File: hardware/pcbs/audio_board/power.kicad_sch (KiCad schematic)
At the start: 31 parts, among them Q1 S8050, U2 LP5907MFX-3.3, U3 LM5158

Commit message: prepare for clock fanout
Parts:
- renumbered R12 to R20, R13 to R21, R14 to R22, R15 to R23, R16 to R24, R17 to R25, R18 to R26

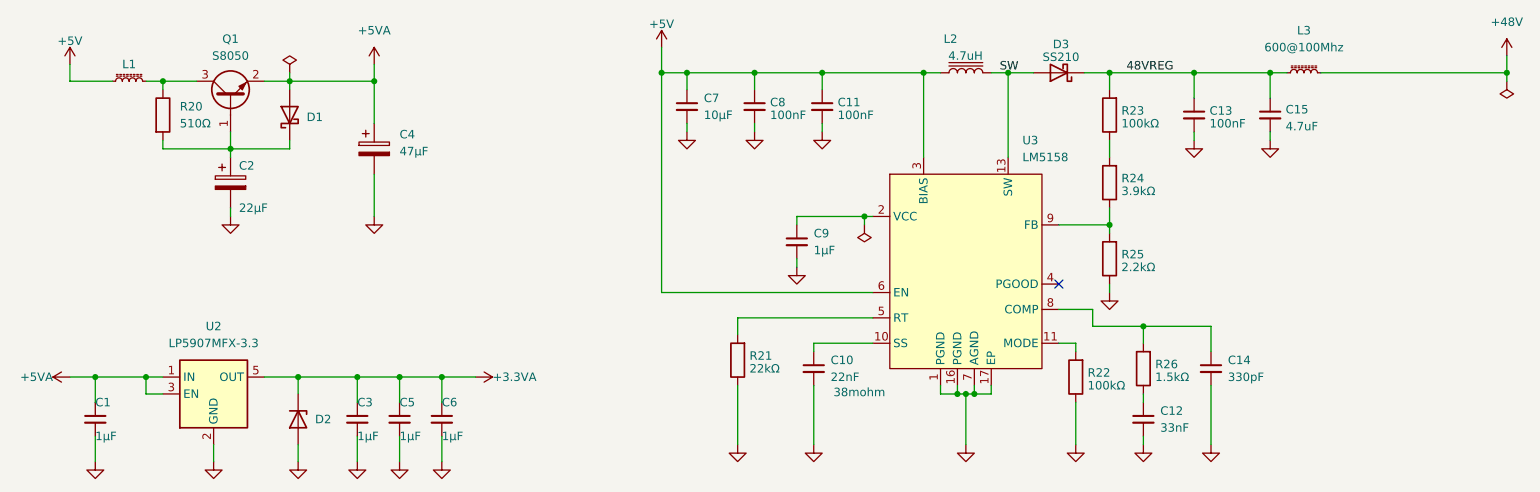
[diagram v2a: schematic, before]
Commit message: audioboard: route clock fanout
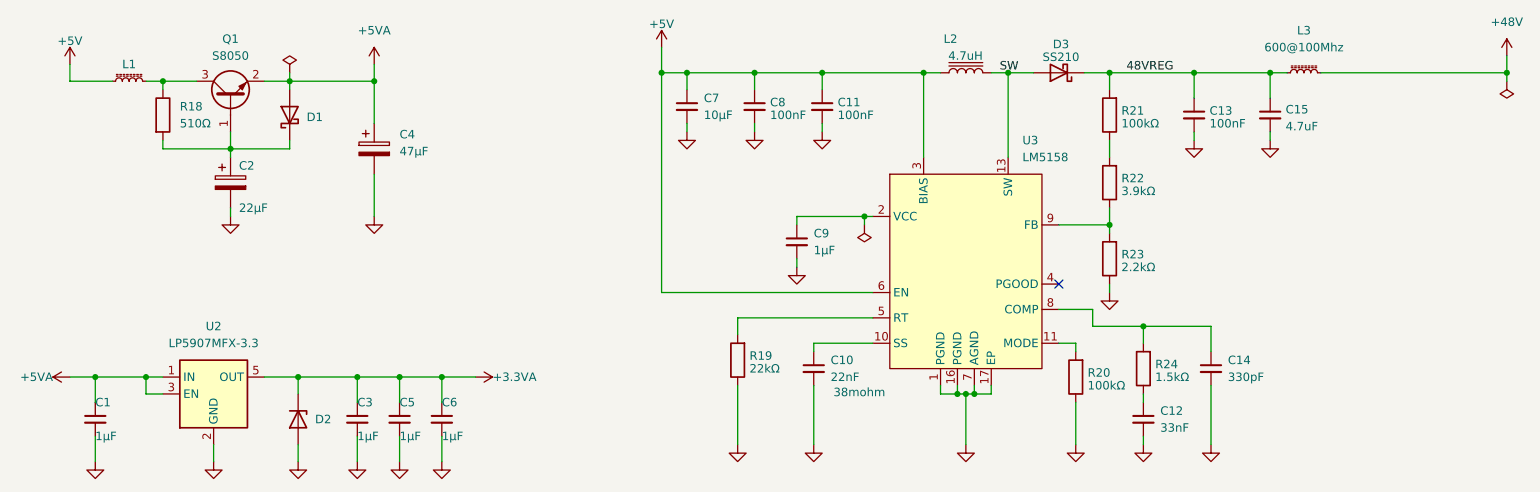
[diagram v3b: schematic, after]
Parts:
- renumbered R20 to R18, R21 to R19, R22 to R20, R23 to R21, R24 to R22, R25 to R23, R26 to R24
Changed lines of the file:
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@@
 		(in_pos_files yes)
 		(dnp no)
-		(property "Reference" "R21"
+		(property "Reference" "R19"
 			(at 147.828 104.7663 0)
 			(show_name no)
@@
 			(project "audio_board"
 				(path "/54443f96-c7c5-4432-b890-45b14a1547a1/23b45e70-9f0d-43c3-ad82-81d9481de3a2"
-					(reference "R21")
+					(reference "R19")
 					(unit 1)
 				)
@@
 		(in_pos_files yes)
 		(dnp no)
-		(property "Reference" "R22"
+		(property "Reference" "R20"
 			(at 198.628 107.3063 0)
 			(show_name no)
@@
 			(project "audio_board"
 				(path "/54443f96-c7c5-4432-b890-45b14a1547a1/23b45e70-9f0d-43c3-ad82-81d9481de3a2"
-					(reference "R22")
+					(reference "R20")
 					(unit 1)
 				)
@@
 		(in_pos_files yes)
 		(dnp no)
-		(property "Reference" "R26"
+		(property "Reference" "R24"
 			(at 208.788 106.0363 0)
 			(show_name no)
@@
 			(project "audio_board"
 				(path "/54443f96-c7c5-4432-b890-45b14a1547a1/23b45e70-9f0d-43c3-ad82-81d9481de3a2"
-					(reference "R26")
+					(reference "R24")
 					(unit 1)
 				)
@@
 		(in_pos_files yes)
 		(dnp no)
-		(property "Reference" "R25"
+		(property "Reference" "R23"
 			(at 203.708 89.5263 0)
 			(show_name no)
@@
 			(project "audio_board"
 				(path "/54443f96-c7c5-4432-b890-45b14a1547a1/23b45e70-9f0d-43c3-ad82-81d9481de3a2"
-					(reference "R25")
+					(reference "R23")
 					(unit 1)
 				)
@@
 		(in_pos_files yes)
 		(dnp no)
-		(property "Reference" "R24"
+		(property "Reference" "R22"
 			(at 203.708 78.0963 0)
 			(show_name no)
@@
 			(project "audio_board"
 				(path "/54443f96-c7c5-4432-b890-45b14a1547a1/23b45e70-9f0d-43c3-ad82-81d9481de3a2"
-					(reference "R24")
+					(reference "R22")
 					(unit 1)
 				)
@@
 		(in_pos_files yes)
 		(dnp no)
-		(property "Reference" "R23"
+		(property "Reference" "R21"
 			(at 203.708 67.9363 0)
 			(show_name no)
@@
 			(project "audio_board"
 				(path "/54443f96-c7c5-4432-b890-45b14a1547a1/23b45e70-9f0d-43c3-ad82-81d9481de3a2"
-					(reference "R23")
+					(reference "R21")
 					(unit 1)
 				)
@@
 		(dnp no)
 		(fields_autoplaced yes)
-		(property "Reference" "R20"
+		(property "Reference" "R18"
 			(at 62.23 67.3099 0)
 			(show_name no)
@@
 			(project "audio_board"
 				(path "/54443f96-c7c5-4432-b890-45b14a1547a1/23b45e70-9f0d-43c3-ad82-81d9481de3a2"
-					(reference "R20")
+					(reference "R18")
 					(unit 1)
 				)

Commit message: audioboard: finalise routing
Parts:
- renumbered R18 to R20, R19 to R21, R20 to R22, R21 to R23, R22 to R24, R23 to R25, R24 to R26

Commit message: minor changes to audioboard
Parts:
- renumbered R20 to R18, R21 to R19, R22 to R20, R23 to R21, R24 to R22, R25 to R23, R26 to R24
